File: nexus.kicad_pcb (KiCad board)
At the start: 2 copper layers, 107 parts, among them J1 PIN6-9_Breakout, J10 Screw_Terminal_01x02, J11 24V_Lockout_Key_Switch, J12 XT60-M, J13 PT_1, J14 PT_4, J15 PT_2, J16 PT_5, J17 PT_3, J18 PT_6, J19 4-Pin Load Cell, J2 PIN10-13_Breakout, J20 5-Pin Load Cell, J21 Ignitor Screw Terminal, J3 Valve_1_PWR, J4 Valve_4_PWR, J5 Valve_2_PWR, J6 Valve_5_PWR, J7 Valve_3_PWR, J8 Valve_6_PWR, J9 Screw_Terminal_01x04, K1 G5LE-1, K2 G5LE-1, Q1 BSS138, Q2 BSS138, Q3 BSS138, Q4 BSS138, Q5 BSS138, Q6 BSS138, Q7 BSS138, Q8 BSS138, U1 ESP32-S3, U2 ADS112C04, U3 ADS112C04, U4 ADS112C04, U5 ADS112C04, U6 XC6206P332MR, U7 TPS5430DDA, U8 TPS5430DDA

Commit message: Satisfy DRC
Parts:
- moved J2 91.2 mm to (205.3, 85.1)
- moved J1 88.8 mm to (205.3, 72.6)
- moved Q2 87.9 mm to (131.7, 95.0)
- moved Q4 87.9 mm to (131.7, 105.0)
- moved Q5 87.9 mm to (131.7, 85.0)
- moved Q6 87.9 mm to (131.7, 115.1)
- moved R10 87.9 mm to (131.2, 108.0)
- moved R11 87.9 mm to (131.2, 89.5)
- moved R13 87.9 mm to (131.2, 88.0)
- moved R14 87.9 mm to (131.2, 118.0)
- moved R20 87.9 mm to (189.6, 114.1)
- moved R36 87.9 mm to (206.4, 143.8)
- moved R4 87.9 mm to (131.2, 99.5)
- moved U7 87.9 mm to (195.7, 35.8)
- moved C2 87.9 mm to (165.5, 117.6)
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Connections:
- U1 pad 0: I2C_SCL -> unconnected-(U1-GPIO0-Pad0)
- U1 pad 1: I2C_SDA -> VALVE_3_CTL
- U1 pad 15: unconnected-(U1-GPIO15/XTAL_32K_P-Pad15) -> I2C_SDA
- U1 pad 16: unconnected-(U1-GPIO16/XTAL_32K_N-Pad16) -> I2C_SCL
- U1 pad 2: VALVE_6_CTL -> VALVE_4_CTL
- U1 pad 38: VALVE_1_CTL -> unconnected-(U1-GPIO38-Pad38)
- U1 pad 39: VALVE_2_CTL -> IGNITOR_CTL
- U1 pad 40: VALVE_3_CTL -> SAFE_24V_CTL
- U1 pad 41: (no net) -> VALVE_6_CTL
- U1 pad 43: unconnected-(U1-GPIO43-Pad43) -> VALVE_1_CTL
- U1 pad 44: unconnected-(U1-GPIO44-Pad44) -> VALVE_2_CTL
- U1 pad 47: IGNITOR_CTL -> unconnected-(U1-GPIO47-Pad47)
- U1 pad 48: SAFE_24V_CTL -> unconnected-(U1-GPIO48-Pad48)
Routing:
- net VALVE_6_CTL: track 0.00 -> 57.7 mm
- net /ESP32 Breakout/PIN8_BREAKOUT: track 0.00 -> 46.8 mm
- net VALVE_5_CTL: track 0.00 -> 45.9 mm
- net /ESP32 Breakout/PIN3_BREAKOUT: track 0.00 -> 43.2 mm
- net /ESP32 Breakout/PIN46_BREAKOUT: track 0.00 -> 39.6 mm
- net /ESP32 Breakout/PIN9_BREAKOUT: track 0.00 -> 36.0 mm
- net VALVE_4_CTL: track 0.00 -> 34.8 mm
- net VALVE_2_CTL: track 0.00 -> 32.3 mm
- net /ESP32 Breakout/PIN10_BREAKOUT: track 0.00 -> 31.4 mm
- net /ESP32 Breakout/PIN11_BREAKOUT: track 0.00 -> 27.8 mm
- net SAFE_24V_CTL: track 0.00 -> 25.4 mm, vias 0 -> 1
- net VALVE_3_CTL: track 0.00 -> 24.9 mm
- net /ESP32 Breakout/PIN12_BREAKOUT: track 0.00 -> 24.2 mm
- net /ESP32 Breakout/PIN13_BREAKOUT: track 0.00 -> 20.7 mm
- net VALVE_1_CTL: track 0.00 -> 19.2 mm
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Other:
- board outline added: 106 x 126.2 mm
- board text added: "ADC1"
- board text added: "ADC1 0 1 2 3"
- board text added: "ADC2"
- board text added: "ADC2 2 3"
- board text added: "ADC3"
- board text added: "ADC4"
- board text added: "LCRUN"
- board text added: "LCTHRUST"
- board text added: "PT1"
- board text added: "PT2"
- board text added: "PT3"
- board text added: "PT4"
- board text added: "PT5"
- board text added: "PT6"

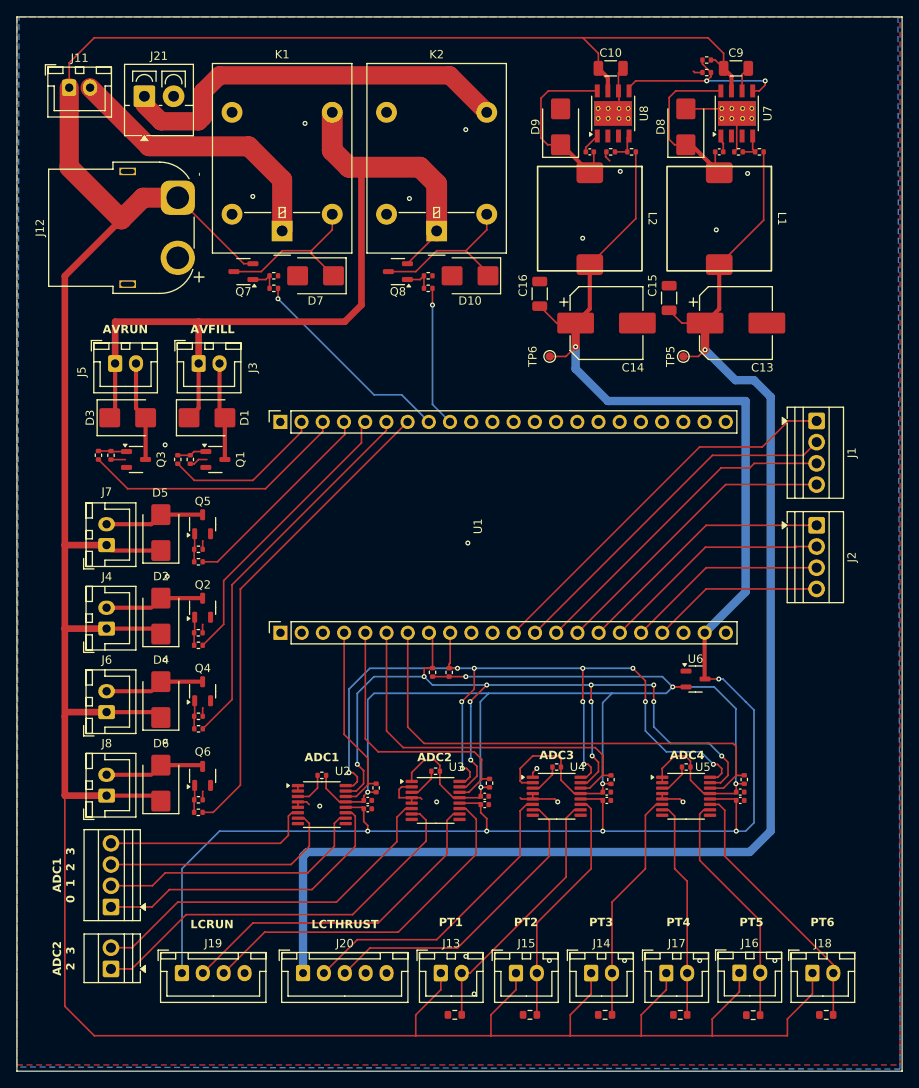
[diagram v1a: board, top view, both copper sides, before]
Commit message: Add Mounting Holes
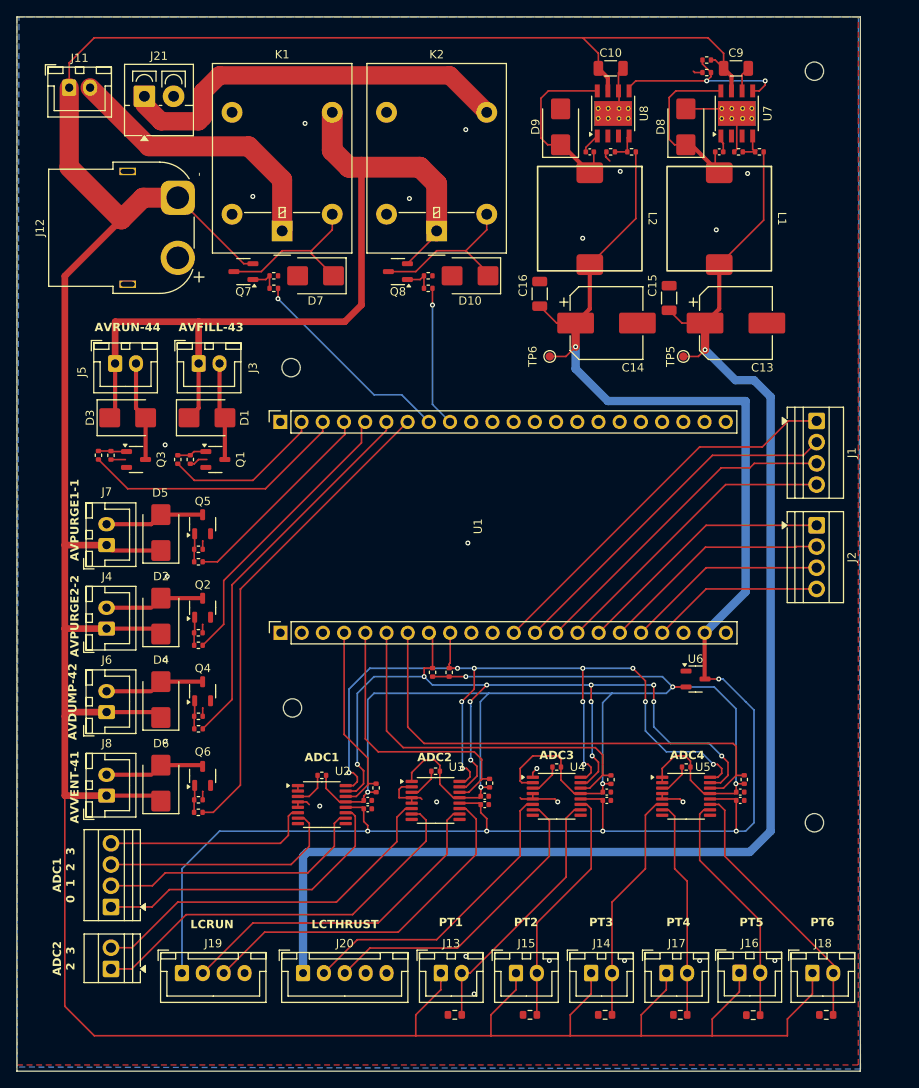
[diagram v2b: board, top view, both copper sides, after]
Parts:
- added REF**: MountingHole_2.2mm_M2, MountingHole:MountingHole_2.2mm_M2, F.Cu at (142.5, 107.0)
- added REF**: MountingHole_2.2mm_M2, MountingHole:MountingHole_2.2mm_M2, F.Cu at (205.0, 120.8)
- added REF**: MountingHole_2.2mm_M2, MountingHole:MountingHole_2.2mm_M2, F.Cu at (205.0, 30.8)
- added REF**: MountingHole_2.2mm_M2, MountingHole:MountingHole_2.2mm_M2, F.Cu at (142.3, 66.2)
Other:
- board size 106 x 126.2 mm -> 101 x 126.2 mm
- board text added: "AVDUMP-42"
- board text added: "AVFILL-43"
- board text added: "AVPURGE1-1"
- board text added: "AVPURGE2-2"
- board text added: "AVRUN-44"
- board text added: "AVVENT-41"
- board text removed: "AVFILL"
- board text removed: "AVRUN"

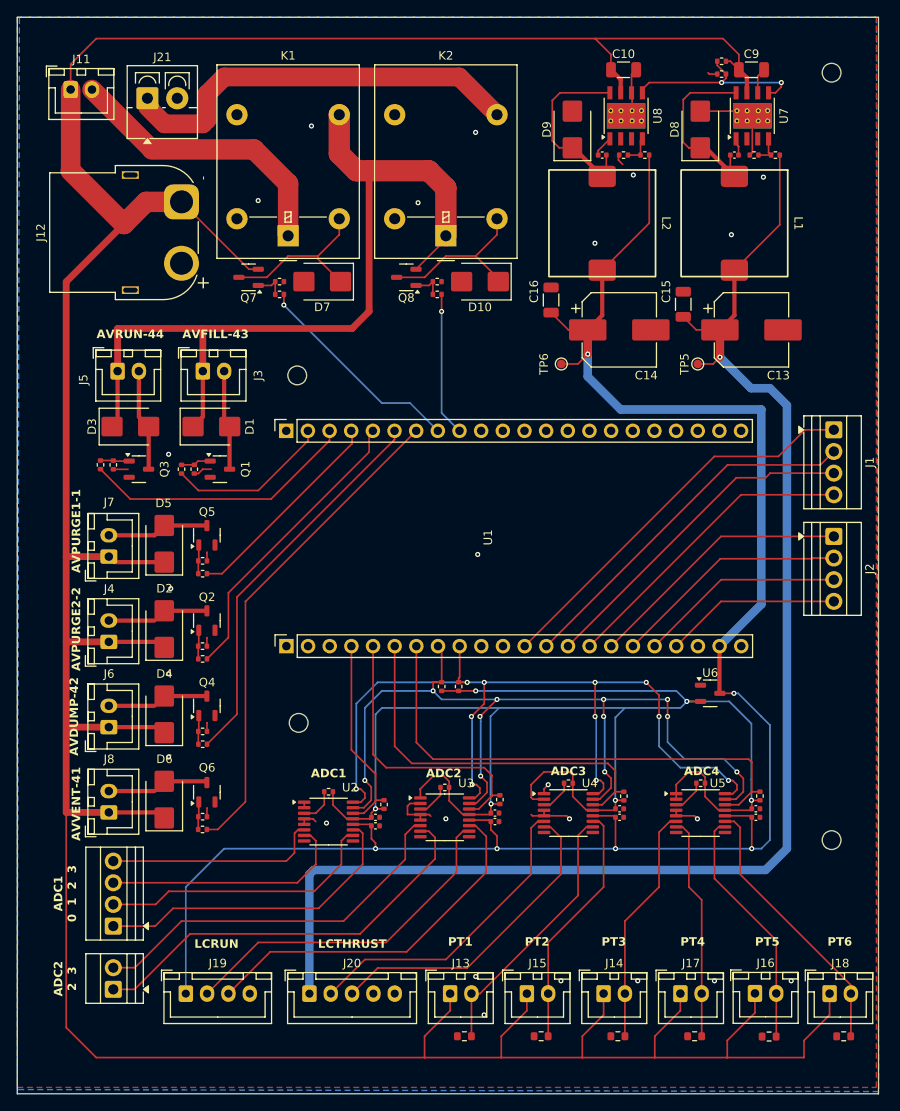
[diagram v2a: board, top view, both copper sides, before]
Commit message: Add silk screening
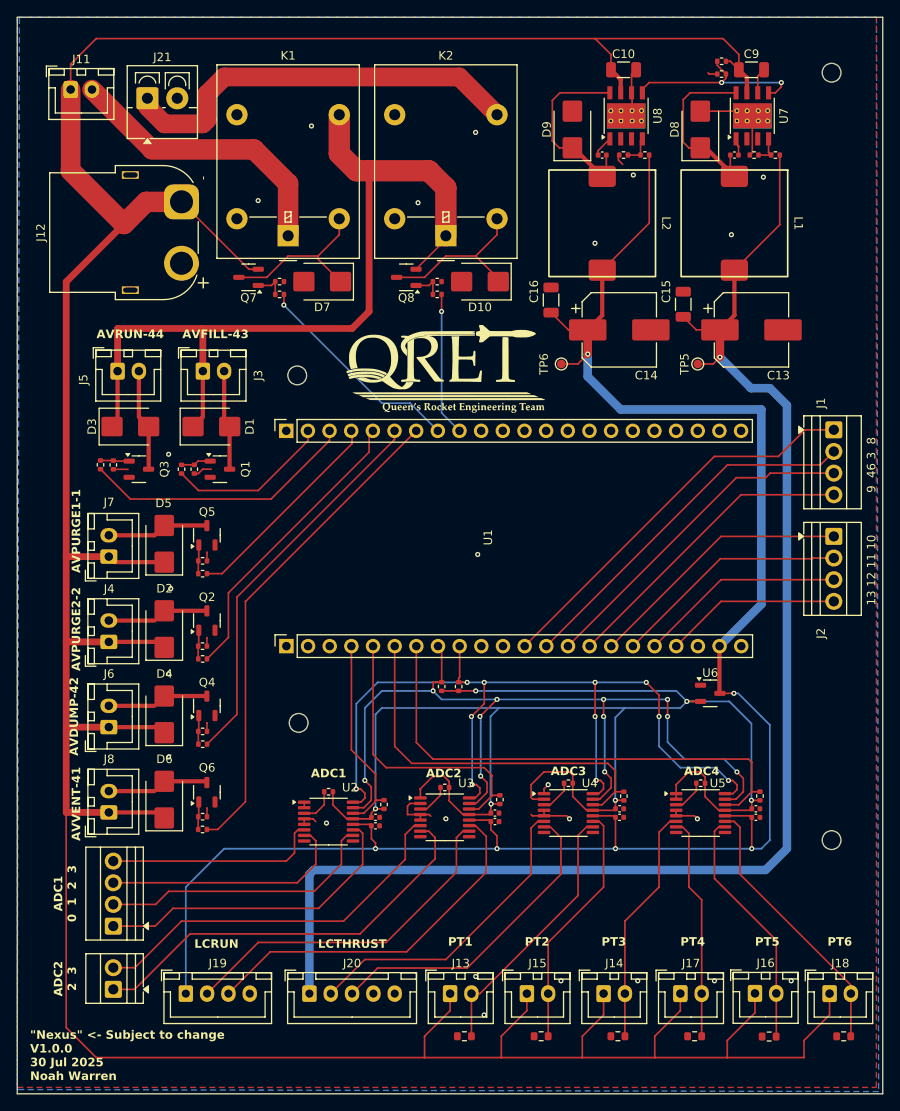
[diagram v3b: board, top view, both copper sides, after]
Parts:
- added G***: LOGO, LOGO, F.Cu at (158.9, 66.1)
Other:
- board size 101 x 126.2 mm -> 101.5 x 126.2 mm
- board text added: "13 12 11 10"
- board text added: "9 46 3 8"
- board text added: "{dblquote}Nexus{dblquote} <- Subject to change V1.0.0 30 Jul 2025 Noah Warren"

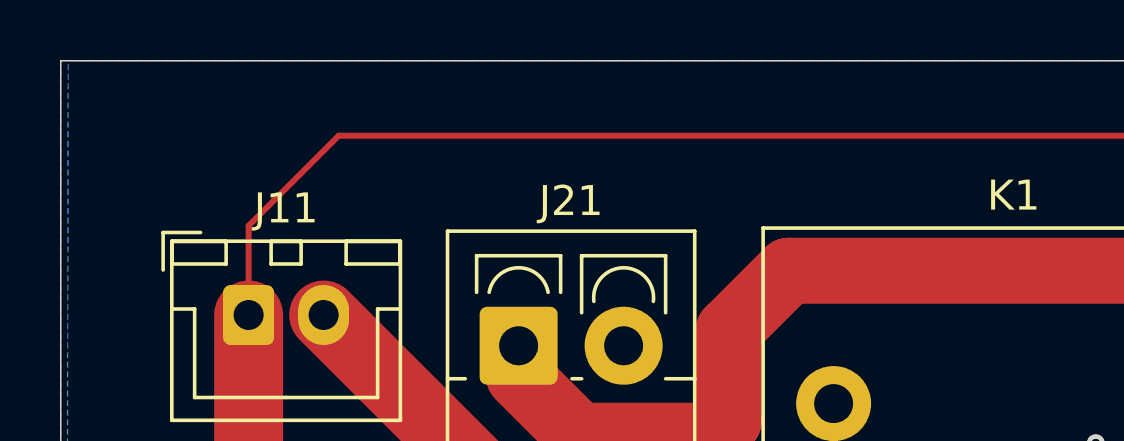
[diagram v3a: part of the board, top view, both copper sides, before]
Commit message: Update silk screening
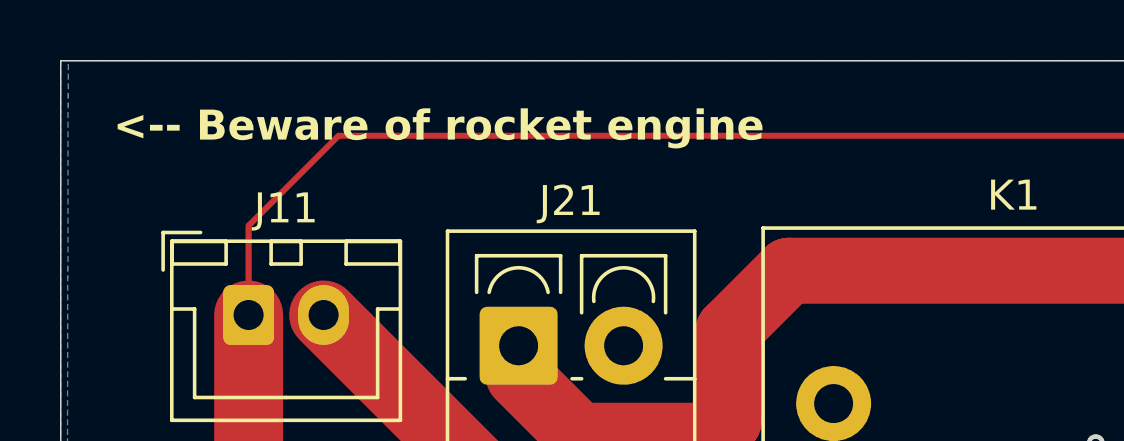
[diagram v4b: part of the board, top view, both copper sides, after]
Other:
- board text added: "<-- Beware of rocket engine"
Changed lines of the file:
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@@
+		)
+	)
+	(gr_text "<-- Beware of rocket engine"
+		(at 111.25 27 0)
+		(layer "F.SilkS")
+		(effects
+			(font
+				(size 1 1)
+				(thickness 0.2)
+				(bold yes)
+			)
+			(justify left bottom)
 		)
 	)

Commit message: PANDA Rebrand
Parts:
- added G***: LOGO, LOGO, F.Cu at (169.0, 85.7)
- added GND: TestPoint_Loop_D2.50mm_Drill1.0mm, TestPoint:TestPoint_Loop_D2.50mm_Drill1.0mm, F.Cu at (206.0, 128.8)
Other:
- board size 101.5 x 126.2 mm -> 100 x 125 mm
- board text added: "<-- Beware of exhaust"
- board text added: "PANDA Propulsion Actuation and Nonsense Data Acquisition V1.0.0 30 Jul 2025 Noah Warren"
- board text removed: "<-- Beware of rocket engine"
- board text removed: "{dblquote}Nexus{dblquote} <- Subject to change V1.0.0 30 Jul 2025 Noah Warren"
